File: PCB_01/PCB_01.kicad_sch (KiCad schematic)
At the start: 48 parts, among them J1 TOUCH_E0, J2 UIM2040PM_Power, J4 UIM2040PM_Signal, J5 BNO055 Adafruit, J6 RAPC712TRP22X, J7 Speaker, J8 UJ20-C-H-G-MSMT-R-4C-P16-TR, Q1 FS8205A, SW1 SW_Push, SW2 SW_Push, SW3 SW_Push, SW4 SW_Push, U1 TP4056, U2 MT3608, U3 MPR121QR2, U4 DFR0299, U5 DW01S

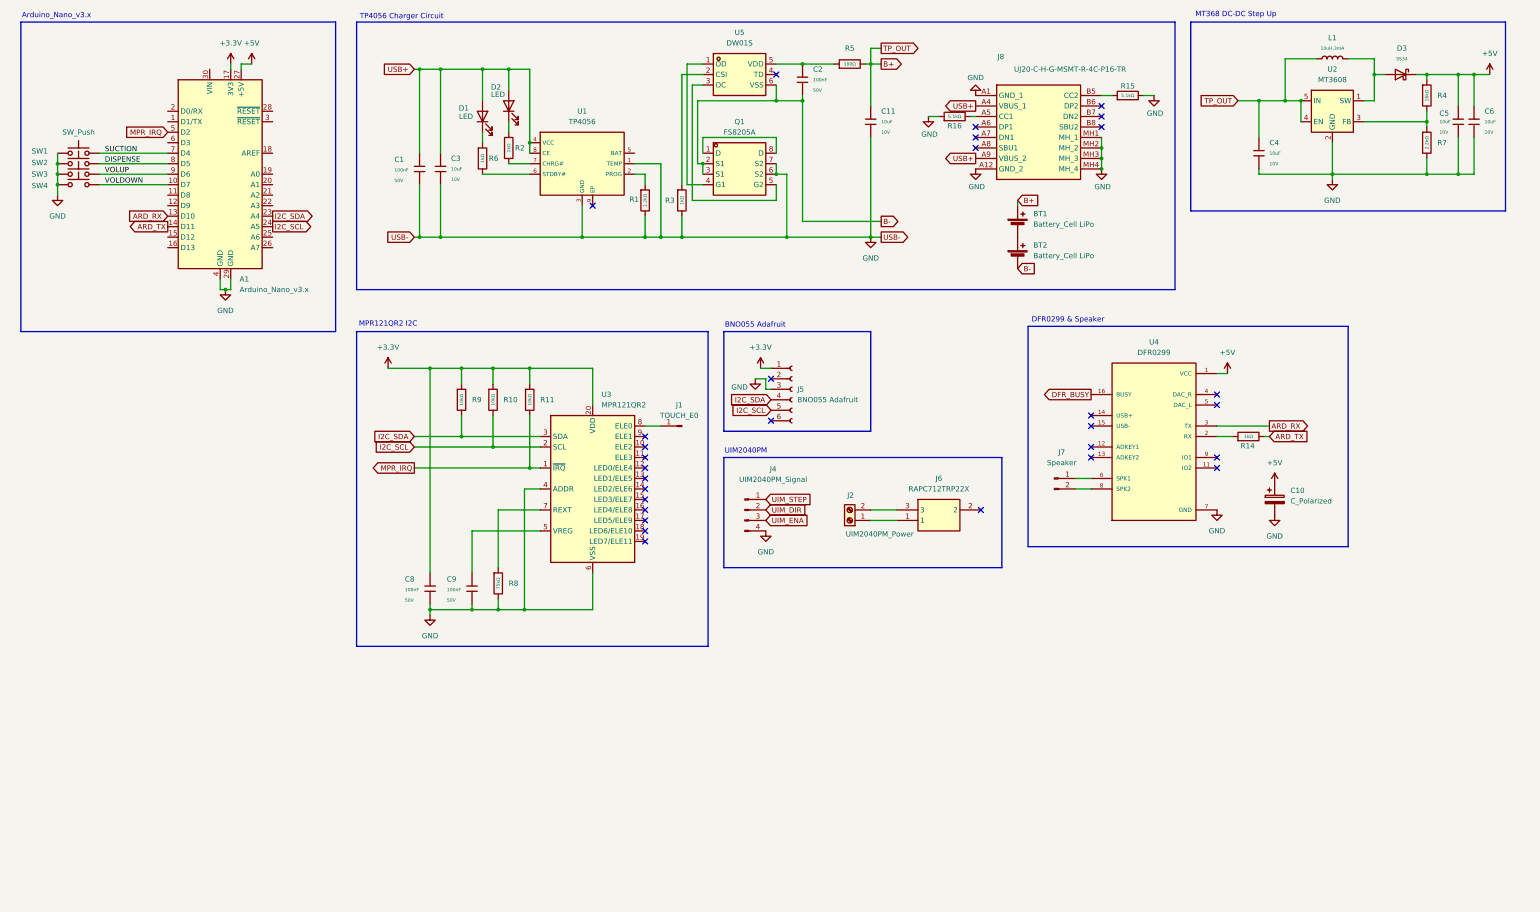
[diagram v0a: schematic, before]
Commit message: Update KiCad PCB layout and schematic, add Molex connector footprints and STEP models, and generate production outputs (BOM, interactive BOM, positions, and fabrication zip files)
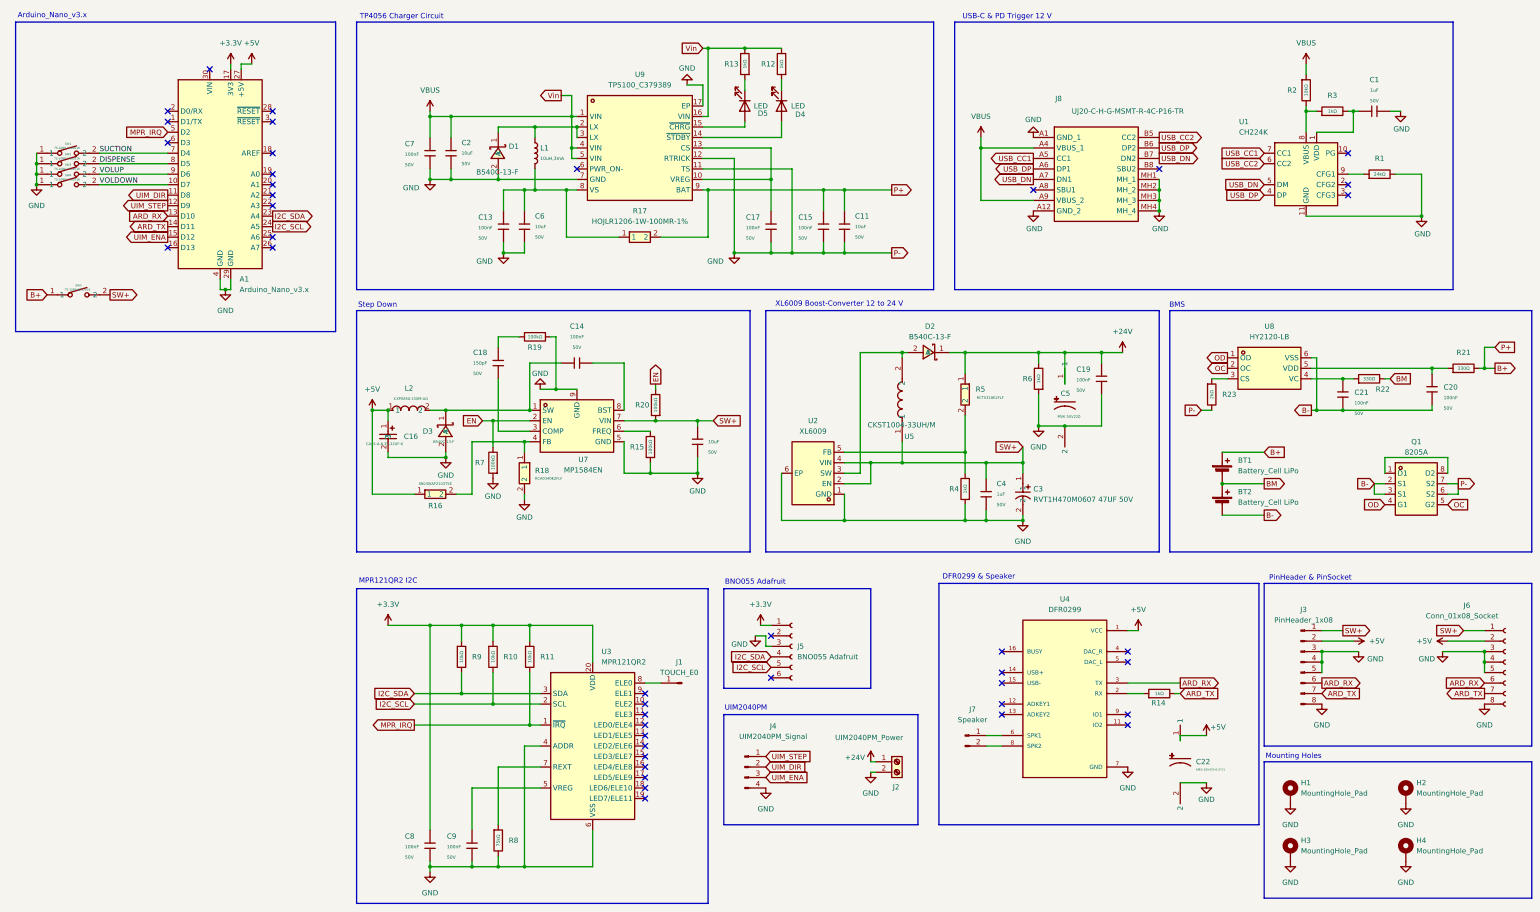
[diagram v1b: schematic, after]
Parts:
- removed C1, C2: 100nF, PCM_JLCPCB:C_0603, symbol PCM_JLCPCB-Capacitors:0603,100nF
- removed C10: C_Polarized, Capacitor_THT:CP_Radial_D8.0mm_P3.50mm, symbol Device:C_Polarized
- removed C11, C3, C4, C5, C6: 10uF, PCM_JLCPCB:C_0603, symbol PCM_JLCPCB-Capacitors:0603,10uF
- removed D1, D2: LED, symbol Device:LED
- removed D3: SS34, PCM_JLCPCB:D_SMA, symbol PCM_JLCPCB-Diodes:Schottky,SS34
- removed J6: RAPC712TRP22X, RAPC712TRP22X, symbol RAPC712TRP22X:RAPC712TRP22X
- removed Q1: FS8205A, FS8205A:TSSOP-8_L4.4-W3.0-P0.65-LS6.4-BL-2, symbol FS8205A:8205A_C14212
- removed R1: 1.2kΩ, PCM_JLCPCB:R_0603, symbol PCM_JLCPCB-Resistors:0603,1.2kΩ
- removed R15, R16: 5.1kΩ, PCM_JLCPCB:R_0603, symbol PCM_JLCPCB-Resistors:0603,5.1kΩ
- removed R2: 1kΩ, PCM_JLCPCB:R_0603, symbol PCM_JLCPCB-Resistors:0603,1kΩ
- removed R4: 16kΩ, PCM_JLCPCB:R_0805, symbol PCM_JLCPCB-Resistors:0805,16kΩ
- removed R5: 100Ω, PCM_JLCPCB:R_0603, symbol PCM_JLCPCB-Resistors:0603,100Ω
- removed R7: 2.2kΩ, PCM_JLCPCB:R_0603, symbol PCM_JLCPCB-Resistors:0603,2.2kΩ
- removed SW1, SW2, SW3, SW4: SW_Push, symbol Switch:SW_Push
- removed U1: TP4056, PCM_JLCPCB:ESOP-8_L4.9-W3.9-P1.27-LS6.0-BL-EP, symbol PCM_JLCPCB-Power:Battery, Li-Ion, 1.0A, TP4056
- removed U2: MT3608, Package_TO_SOT_SMD:SOT-23-6, symbol Regulator_Switching:MT3608
- removed U5: DW01S, DW01S:SOT-23-6_L2.9-W1.6-P0.95-LS2.8-BR, symbol DW01S:DW01S
- added C1, C4: 1uF, PCM_JLCPCB:C_0603, symbol PCM_JLCPCB-Capacitors:0603,1uF
- added C11, C12, C2, C6: 10uF, PCM_JLCPCB:C_1206, symbol PCM_JLCPCB-Capacitors:1206,10uF
- added C13, C14, C15, C17, C19, C20, C21, C7: 100nF, PCM_JLCPCB:C_0603, symbol PCM_JLCPCB-Capacitors:0603,100nF
- added C16: CA45-A-6.3V-22UF-K, EasyEDA:CASE-A_3216, symbol EasyEDA:CA45-A-6.3V-22UF-K
- added C18: 150pF, PCM_JLCPCB:C_0603, symbol PCM_JLCPCB-Capacitors:0603,150pF
- added C22: KMG-10V470-6.3*11, EasyEDA:CAP-TH_BD6.3-P2.50-D1.0-FD, symbol EasyEDA:KMG-10V470-6.3*11
- added C3: RVT1H470M0607 47UF 50V, EasyEDA:CAP-SMD_BD6.3-L6.6-W6.6-LS7.2-FD, symbol EasyEDA:RVT1H470M060747UF50V
- added C5: MVK 50V220, EasyEDA:CAP-SMD_BD10.0-L10.3-W10.3-FD, symbol EasyEDA:MVK50V220
- added D1, D2, D3: B540C-13-F, EasyEDA:SMC_L7.1-W6.2-LS8.1-RD, symbol EasyEDA:B540C-13-F
- added D4, D5: LED, LED_SMD:LED_0805_2012Metric, symbol Device:LED
- added H1, H2, H3, H4: MountingHole_Pad, MountingHole:MountingHole_2.2mm_M2_DIN965_Pad, symbol Mechanical:MountingHole_Pad
- added J3: PinHeader_1x08, Connector_PinHeader_1.00mm:PinHeader_1x08_P1.00mm_Vertical, symbol Connector:Conn_01x08_Pin
- added J6: Conn_01x08_Socket, Connector_PinSocket_1.00mm:PinSocket_1x08_P1.00mm_Vertical, symbol Connector:Conn_01x08_Socket
- added L2: CXP0850-150M-AG, EasyEDA:IND-SMD_L8.5-W8.0_PCC-M0854M, symbol EasyEDA:CXP0850-150M-AG
- added Q1: 8205A, EasyEDA:TSSOP-8_L4.4-W3.0-P0.65-LS6.4-BL, symbol EasyEDA:8205A
- added R1: 24kΩ, PCM_JLCPCB:R_0603, symbol PCM_JLCPCB-Resistors:0603,24kΩ
- added R12, R13, R4: 1kΩ, PCM_JLCPCB:R_0603, symbol PCM_JLCPCB-Resistors:0603,1kΩ
- added R15, R19, R20, R7: 100kΩ, PCM_JLCPCB:R_0603, symbol PCM_JLCPCB-Resistors:0603,100kΩ
- added R16: 0603WAF2103T5E, EasyEDA:R0603, symbol EasyEDA:0603WAF2103T5E
- added R17: HOJLR1206-1W-100MR-1%, EasyEDA:RES-SMD_L3.2-W1.6_SY1206, symbol EasyEDA:HOJLR1206-1W-100MR-1%
- added R18: RCA0340K2FLF, EasyEDA:R0603, symbol EasyEDA:RCA0340K2FLF
- added R2: 10kΩ, PCM_JLCPCB:R_0603, symbol PCM_JLCPCB-Resistors:0603,10kΩ
- added R21, R22: 330Ω, PCM_JLCPCB:R_0603, symbol PCM_JLCPCB-Resistors:0603,330Ω
- added R23: 2kΩ, PCM_JLCPCB:R_0603, symbol PCM_JLCPCB-Resistors:0603,2kΩ
- added R5: RCT0318K2FLF, EasyEDA:R0603, symbol EasyEDA:RCT0318K2FLF
- added SW1, SW2, SW3, SW4, SW5: TS-1088-AR02016, EasyEDA:SW-SMD_L3.9-W3.0-P4.45, symbol EasyEDA:TS-1088-AR02016
- added U1: CH224K, Package_SO:SSOP-10-1EP_3.9x4.9mm_P1mm_EP2.1x3.3mm, symbol Interface_USB:CH224K
- added U2: XL6009, EasyEDA:TO-263-5_L10.2-W8.6-P1.70-LS14.4-TL, symbol EasyEDA:XL6009
- added U5: CKST1004-33UH/M, EasyEDA:IND-SMD_L11.6-W10.1, symbol EasyEDA:CKST1004-33UH_M
- added U7: MP1584EN, EasyEDA:SOIC-8_L4.9-W3.9-P1.27-LS6.0-BL-EP3.3, symbol EasyEDA:MP1584EN
- added U8: HY2120-LB, EasyEDA:SOT-23-6_L2.9-W1.6-P0.95-LS2.8-BR, symbol EasyEDA:HY2120-LB
- added U9: TP5100_C379389, EasyEDA:TQFN-16_L4.0-W4.0-P0.65-BL-EP, symbol TP5100:TP5100_C379389
- J7: footprint (none) -> Connector_JST:JST_PH_S2B-PH-K_1x02_P2.00mm_Horizontal
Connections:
- net +5V: now also C16.1, C22.1, J3.2 (Pin_2), J6.2 (Pin_2), L2.1, R16.1
- net ARD_RX: now also J3.6 (Pin_6), J6.6 (Pin_6)
- net ARD_TX: now also J3.7 (Pin_7), J6.7 (Pin_7)
- net B+: now also C11.1, C15.1, R17.2, R21.2, SW5.1, U9.9 (BAT); no longer L1.1
- net B-: now also C20.2, C21.2, Q1.2 (S1), Q1.3 (S1), U8.6 (VSS)
- net DISPENSE: now also SW2.2
- net GND: now also J2.2 (Pin_2), R6.1, C1.1, C11.2, C12.2, C13.2, C15.2, C16.2, C17.2, C19.2, C2.2, C22.2, C3.2, C4.2, C5.2, C6.2, C7.2, D1.2 (A), D3.2 (A), H1.1, H2.1, H3.1, H4.1, J3.3 (Pin_3), J3.4 (Pin_4), J3.5 (Pin_5), J3.8 (Pin_8), J6.3 (Pin_3), J6.4 (Pin_4), J6.5 (Pin_5), J6.8 (Pin_8), Q1.6 (S2), Q1.7 (S2), R1.2, R15.1, R18.2, R19.1, R23.2, R4.1, R7.1, SW1.1, SW2.1, SW3.1, SW4.1, U1.11 (GND), U2.1 (GND), U2.6 (EP), U7.5 (GND), U7.9 (GND), U9.11 (TS), U9.12 (RTRICK), U9.17 (EP), U9.7 (GND); no longer R3.2
- net SUCTION: now also SW1.2
- net UIM_DIR: now also A1.11 (D8)
- net UIM_ENA: now also A1.15 (D12)
- net UIM_STEP: now also A1.12 (D9)
- net VOLDOWN: now also SW4.2
- net VOLUP: now also SW3.2
- net USB_CC2: now reaches J8.B5 (CC2)
- net USB_CC2: now also U1.6 (CC2)
- net +24V: now reaches R6.2
- net +24V: now also J2.1 (Pin_1), C19.1, C5.1, D2.1 (K), R5.1
- net at L1.2: now also C13.1, C6.1, R17.1, U9.8 (VS)
- net BM: now reaches BT1.2 (-), BT2.1 (+)
- net BM: now also R22.2
- net at R3.1: now also R2.2, U1.8 (VBUS)
- net USB_CC1: now reaches J8.A5 (CC1)
- net USB_CC1: now also U1.7 (CC1)
- net USB_DP: now reaches J8.A6 (DP1)
- net USB_DP: now also J8.B6 (DP2), U1.4 (DP)
- net USB_DN: now reaches J8.A7 (DN1)
- net USB_DN: now also J8.B7 (DN2), U1.5 (DM)
- net DFR_BUSY: no longer names the net of U4.16 (BUSY)
- net USB+ renamed VBUS
- net VBUS: now also C2.1, C7.1, R12.2, R13.2, R2.1, U9.1 (VIN), U9.16 (VIN), U9.4 (VIN), U9.5 (VIN)
- new net: R16.2, R18.1, U7.4 (FB)
- new net: D4.1 (K), R12.1
- new net: D4.2 (A), U9.14 (~{STDBY})
- new net: C21.1, R22.1, U8.4 (VC)
- new net: R1.1, U1.9 (CFG1)
- new net: D5.1 (K), R13.1
- new net: C1.2, R3.2, U1.1 (VDD)
- new net: C20.1, R21.1, U8.5 (VDD)
- new net: D2.2 (A), U2.3 (SW), U5.2
- new net: C17.1, U9.10 (VREG), U9.13 (CS)
- new net: C14.1, D3.1 (K), L2.2, U7.1 (SW)
- new net: C18.2, U7.3 (COMP)
- new net: R15.2, U7.6 (FREQ)
- new net: C14.2, U7.8 (BST)
- new net: R4.2, R5.2, U2.5 (FB)
- new net: R23.1, U8.3 (CS)
- new net: D5.2 (A), U9.15 (~{CHRG})
- new net: D1.1 (K), L1.1, U9.2 (LX), U9.3 (LX)
- new net: C18.1, R19.2
- new net: Q1.1 (D1), Q1.8 (D2)
- new net EN: R20.2, R7.2, U7.2 (EN)
- new net OC: Q1.5 (G2), U8.2 (OC)
- new net OD: Q1.4 (G1), U8.1 (OD)
- new net SW+: C12.1, C3.1, C4.1, J3.1 (Pin_1), J6.1 (Pin_1), R20.1, SW5.2, U2.2 (EN), U2.4 (VIN), U5.1, U7.7 (VIN)
- no-connect marks 30 -> 42
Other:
- note added: "BMS"
- note added: "Mounting Holes"
- note added: "PinHeader & PinSocket"
- note added: "Step Down"
- note added: "USB-C & PD Trigger 12 V"
- note added: "XL6009 Boost-Converter 12 to 24 V"
- note removed: "MT368 DC-DC Step Up"
- moved on the sheet: BT1, BT2, C8, C9, J1, J2, J4, J5, J7, J8, R10, R11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
